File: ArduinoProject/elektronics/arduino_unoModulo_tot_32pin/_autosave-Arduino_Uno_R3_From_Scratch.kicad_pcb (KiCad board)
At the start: 2 copper layers, 68.9 x 47.8 mm, 36 parts, among them IC401 MC33269ST-5.OT3, IC402 MC33269ST-5.OT3, J201 POWER, J202 IOL, J203 IOL, J204 IOL, SW601 RESET_SWITCH, U301 74AHC1G04, U302 L298D, U303 74AHC1G04, U601 ATMEGA328P-MU20, X1 DG3XX-04-3.5, X2 DG3XX-02-3.5, Y601 Crystal

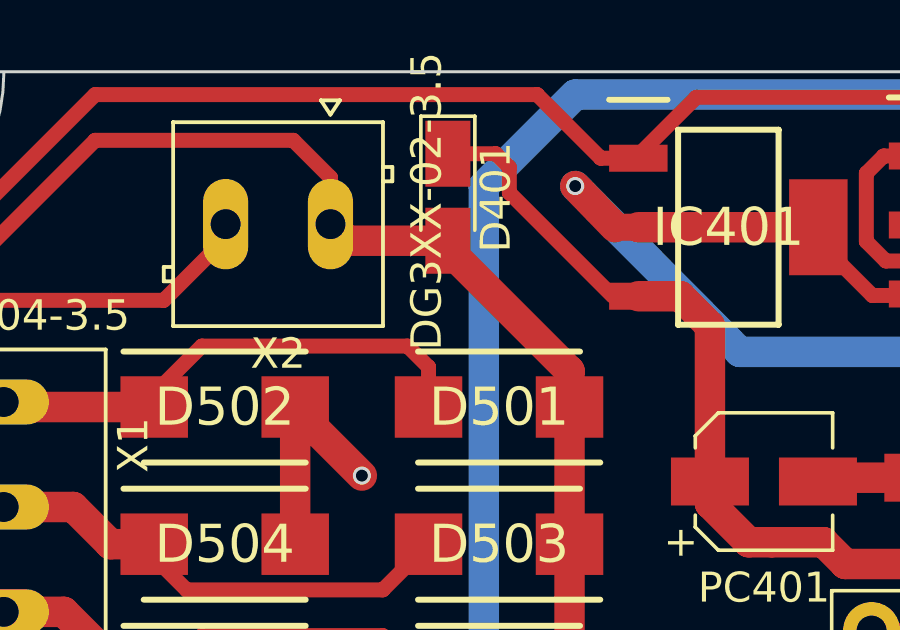
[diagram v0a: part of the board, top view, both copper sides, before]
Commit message: diode changed
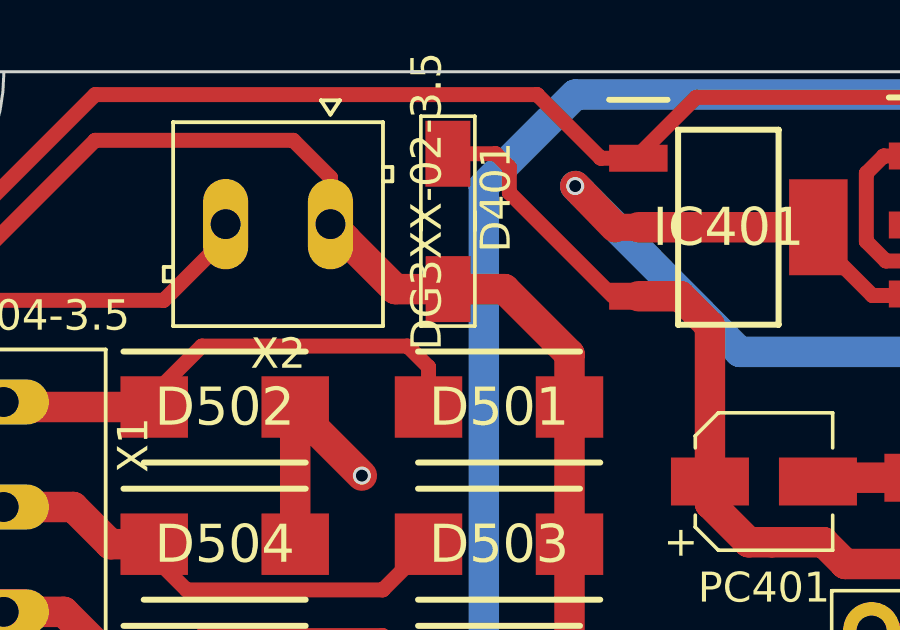
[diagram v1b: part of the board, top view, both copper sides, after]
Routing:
- net /L298_Driver./PWRIN: track 83.5 -> 84.4 mm
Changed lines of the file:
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@@
     (thickness 1.6)
     (drawings 17)
-    (tracks 562)
+    (tracks 563)
     (zones 0)
     (modules 36)
@@
   (layers
     (0 F.Cu signal)
-    (31 B.Cu signal)
+    (31 B.Cu signal hide)
     (32 B.Adhes user)
     (33 F.Adhes user hide)
@@
     (uvia_dia 0.3)
     (uvia_drill 0.1)
-  )
-  (net_class twentymill ""
-    (clearance 0.2)
-    (trace_width 0.5)
-    (via_dia 0.6)
-    (via_drill 0.4)
-    (uvia_dia 0.3)
-    (uvia_drill 0.1)
     (add_net +5V)
     (add_net /ATMEGA328P/AD0)
@@
     (add_net "Net-(U302-Pad18)")
     (add_net "Net-(U302-Pad3)")
+  )
+  (net_class twentymill ""
+    (clearance 0.2)
+    (trace_width 0.5)
+    (via_dia 0.6)
+    (via_drill 0.4)
+    (uvia_dia 0.3)
+    (uvia_drill 0.1)
+  )
+  (module Diodes_SMD:D_MicroMELF_Hadsoldering (layer F.Cu)
+    (at 162.31 96.696 270)
+    (descr "Diode, MicroMELF, hand-soldering, http://www.vishay.com/docs/85597/bzm55-se.pdf")
+    (tags "MicroMELF Diode")
+    (attr smd)
+    (fp_text reference D401 (at 0 -1.6 270) (layer F.SilkS)
+      (effects (font (size 1 1) (thickness 0.15)))
+    )
+    (fp_text value D (at 0 1.55 270) (layer F.Fab)
+      (effects (font (size 1 1) (thickness 0.15)))
+    )
+    (fp_line (start 4.44592 1) (end -1.15408 1) (layer F.CrtYd) (width 0.05))
+    (fp_line (start -1.1236 -1) (end 4.4764 -1) (layer F.CrtYd) (width 0.05))
+    (fp_line (start 4.29516 -0.89492) (end 4.29516 0.90508) (layer F.SilkS) (width 0.12))
+    (fp_line (start 0.49532 0.9) (end 4.29532 0.9) (layer F.SilkS) (width 0.12))
+    (fp_line (start 4.28516 -0.9) (end 0.48516 -0.9) (layer F.SilkS) (width 0.12))
+    (fp_text user %R (at 0 -1.6 270) (layer F.Fab)
+      (effects (font (size 1 1) (thickness 0.15)))
+    )
+    (fp_line (start 1.1 -0.9) (end -2.7 -0.9) (layer F.SilkS) (width 0.12))
+    (fp_line (start -2.7 -0.9) (end -2.7 0.9) (layer F.SilkS) (width 0.12))
+    (fp_line (start -2.7 0.9) (end 1.1 0.9) (layer F.SilkS) (width 0.12))
+    (fp_line (start 0.25 0) (end 0.75 0) (layer F.Fab) (width 0.12))
+    (fp_line (start -0.25 0) (end 0.25 -0.25) (layer F.Fab) (width 0.12))
+    (fp_line (start 0.25 -0.25) (end 0.25 0.25) (layer F.Fab) (width 0.12))
+    (fp_line (start 0.25 0.25) (end -0.25 0) (layer F.Fab) (width 0.12))
+    (fp_line (start -0.25 0) (end -0.75 0) (layer F.Fab) (width 0.12))
+    (fp_line (start -0.25 -0.25) (end -0.25 0.25) (layer F.Fab) (width 0.12))
+    (fp_line (start -0.6 -0.55) (end -0.6 0.55) (layer F.Fab) (width 0.12))
+    (fp_line (start -1.1 -0.55) (end 1.1 -0.55) (layer F.Fab) (width 0.12))
+    (fp_line (start 1.1 -0.55) (end 1.1 0.55) (layer F.Fab) (width 0.12))
+    (fp_line (start 1.1 0.55) (end -1.1 0.55) (layer F.Fab) (width 0.12))
+    (fp_line (start -1.1 0.55) (end -1.1 -0.55) (layer F.Fab) (width 0.12))
+    (fp_line (start -2.8 -1) (end 2.8 -1) (layer F.CrtYd) (width 0.05))
+    (fp_line (start -2.8 -1) (end -2.8 1) (layer F.CrtYd) (width 0.05))
+    (fp_line (start 4.44084 0.96952) (end 4.44084 -1.03048) (layer F.CrtYd) (width 0.05))
+    (fp_line (start 2.8 1) (end -2.8 1) (layer F.CrtYd) (width 0.05))
+    (pad 1 smd rect (at -1.45 0 270) (size 2.2 1.5) (layers F.Cu F.Paste F.Mask)
+      (net 6 /Headers/VIN))
+    (pad 2 smd rect (at 3.06324 -0.01016 270) (size 2.2 1.5) (layers F.Cu F.Paste F.Mask)
+      (net 1 /L298_Driver./PWRIN))
+    (model ${KISYS3DMOD}/Diodes_SMD.3dshapes/D_MicroMELF.wrl
+      (at (xyz 0 0 0))
+      (scale (xyz 1 1 1))
+      (rotate (xyz 0 0 0))
+    )
   )
   (module Socket_Strips:Socket_Strip_Straight_1x08_Pitch2.54mm (layer F.Cu)
@@
       (net 4 /Headers/+3V3))
   )
-  (module Diodes_SMD:D_MicroMELF_Hadsoldering (layer F.Cu)
-    (at 162.31 96.696 270)
-    (descr "Diode, MicroMELF, hand-soldering, http://www.vishay.com/docs/85597/bzm55-se.pdf")
-    (tags "MicroMELF Diode")
-    (attr smd)
-    (fp_text reference D401 (at 0 -1.6 270) (layer F.SilkS)
-      (effects (font (size 1 1) (thickness 0.15)))
-    )
-    (fp_text value D (at 0 1.55 270) (layer F.Fab)
-      (effects (font (size 1 1) (thickness 0.15)))
-    )
-    (fp_text user %R (at 0 -1.6 270) (layer F.Fab)
-      (effects (font (size 1 1) (thickness 0.15)))
-    )
-    (fp_line (start 1.1 -0.9) (end -2.7 -0.9) (layer F.SilkS) (width 0.12))
-    (fp_line (start -2.7 -0.9) (end -2.7 0.9) (layer F.SilkS) (width 0.12))
-    (fp_line (start -2.7 0.9) (end 1.1 0.9) (layer F.SilkS) (width 0.12))
-    (fp_line (start 0.25 0) (end 0.75 0) (layer F.Fab) (width 0.12))
-    (fp_line (start -0.25 0) (end 0.25 -0.25) (layer F.Fab) (width 0.12))
-    (fp_line (start 0.25 -0.25) (end 0.25 0.25) (layer F.Fab) (width 0.12))
-    (fp_line (start 0.25 0.25) (end -0.25 0) (layer F.Fab) (width 0.12))
-    (fp_line (start -0.25 0) (end -0.75 0) (layer F.Fab) (width 0.12))
-    (fp_line (start -0.25 -0.25) (end -0.25 0.25) (layer F.Fab) (width 0.12))
-    (fp_line (start -0.6 -0.55) (end -0.6 0.55) (layer F.Fab) (width 0.12))
-    (fp_line (start -1.1 -0.55) (end 1.1 -0.55) (layer F.Fab) (width 0.12))
-    (fp_line (start 1.1 -0.55) (end 1.1 0.55) (layer F.Fab) (width 0.12))
-    (fp_line (start 1.1 0.55) (end -1.1 0.55) (layer F.Fab) (width 0.12))
-    (fp_line (start -1.1 0.55) (end -1.1 -0.55) (layer F.Fab) (width 0.12))
-    (fp_line (start -2.8 -1) (end 2.8 -1) (layer F.CrtYd) (width 0.05))
-    (fp_line (start -2.8 -1) (end -2.8 1) (layer F.CrtYd) (width 0.05))
-    (fp_line (start 2.8 1) (end 2.8 -1) (layer F.CrtYd) (width 0.05))
-    (fp_line (start 2.8 1) (end -2.8 1) (layer F.CrtYd) (width 0.05))
-    (pad 1 smd rect (at -1.45 0 270) (size 2.2 1.5) (layers F.Cu F.Paste F.Mask)
-      (net 6 /Headers/VIN))
-    (pad 2 smd rect (at 1.45 0 270) (size 2.2 1.5) (layers F.Cu F.Paste F.Mask)
-      (net 1 /L298_Driver./PWRIN))
-    (model ${KISYS3DMOD}/Diodes_SMD.3dshapes/D_MicroMELF.wrl
-      (at (xyz 0 0 0))
-      (scale (xyz 1 1 1))
-      (rotate (xyz 0 0 0))
-    )
-  )
   (module SK25AHM2G:DIOM5437X240N (layer F.Cu)
     (at 164.016 103.689 180)
@@
   (gr_line (start 141.41 92.513) (end 197.544 92.513) (angle 90) (layer Edge.Cuts) (width 0.1))
   (gr_line (start 141.288 92.456) (end 141.288 140.208) (angle 90) (layer Edge.Cuts) (width 0.1))
+  (segment (start 162.32016 99.75924) (end 160.56376 99.75924) (width 1.016) (layer F.Cu) (net 1))
+  (segment (start 160.56376 99.75924) (end 158.39752 97.593) (width 1.016) (layer F.Cu) (net 1))
+  (segment (start 166.366 103.689) (end 166.366 101.927) (width 1.016) (layer F.Cu) (net 1))
+  (segment (start 164.19824 99.75924) (end 162.32016 99.75924) (width 1.016) (layer F.Cu) (net 1))
+  (segment (start 166.366 101.927) (end 164.19824 99.75924) (width 1.016) (layer F.Cu) (net 1))
   (segment (start 152.146 129.454) (end 148.379 129.454) (width 0.5) (layer F.Cu) (net 1))
+  (segment (start 148.379 129.454) (end 142.934 124.009) (width 0.5) (layer F.Cu) (net 1))
+  (segment (start 142.934 124.009) (end 142.934 102.419) (width 0.5) (layer F.Cu) (net 1))
+  (segment (start 142.934 102.419) (end 150.554 94.799) (width 0.5) (layer F.Cu) (net 1))
+  (segment (start 150.554 94.799) (end 157.158 94.799) (width 0.5) (layer F.Cu) (net 1))
+  (segment (start 157.158 94.799) (end 158.39752 96.03852) (width 0.5) (layer F.Cu) (net 1))
   (segment (start 158.39752 96.03852) (end 158.39752 97.593) (width 0.5) (layer F.Cu) (net 1))
-  (segment (start 157.158 94.799) (end 158.39752 96.03852) (width 0.5) (layer F.Cu) (net 1))
-  (segment (start 150.554 94.799) (end 157.158 94.799) (width 0.5) (layer F.Cu) (net 1))
-  (segment (start 142.934 102.419) (end 150.554 94.799) (width 0.5) (layer F.Cu) (net 1))
-  (segment (start 142.934 124.009) (end 142.934 102.419) (width 0.5) (layer F.Cu) (net 1))
-  (segment (start 148.379 129.454) (end 142.934 124.009) (width 0.5) (layer F.Cu) (net 1))
-  (segment (start 162.31 98.146) (end 158.95052 98.146) (width 1.016) (layer F.Cu) (net 1))
   (segment (start 158.95052 98.146) (end 158.39752 97.593) (width 1.016) (layer F.Cu) (net 1))
-  (segment (start 166.366 103.689) (end 166.366 102.483) (width 1.016) (layer F.Cu) (net 1))
-  (segment (start 166.366 102.483) (end 162.31 98.427) (width 1.016) (layer F.Cu) (net 1))
-  (segment (start 162.31 98.427) (end 162.31 98.146) (width 1.016) (layer F.Cu) (net 1))
   (segment (start 166.366 108.261) (end 166.366 103.689) (width 1.016) (layer F.Cu) (net 1))
   (segment (start 166.366 112.833) (end 166.366 108.261) (width 1.016) (layer F.Cu) (net 1))
